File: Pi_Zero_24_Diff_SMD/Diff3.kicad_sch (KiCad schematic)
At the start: 14 parts, among them J10 Diff Out, J9 Diff Out, U10 AM26C31, U9 AM26C31

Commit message: generated WIP PCB
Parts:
- C10, C11: footprint (none) -> Capacitor_SMD:C_0603_1608Metric_Pad1.08x0.95mm_HandSolder
- J10, J9: footprint (none) -> Scotts:RJ45_Amphenol_54602-x08_Horizontal
- R22, R23, R24, R25, R26, R27, R28, R29: footprint (none) -> Resistor_SMD:R_0603_1608Metric_Pad0.98x0.95mm_HandSolder
- U10, U9: footprint (none) -> Package_SO:SOIC-16_3.9x9.9mm_P1.27mm
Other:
- title: Pi_Zero_24_Diff -> Pi Zero 24 Diff
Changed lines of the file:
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@@
   (paper "A4")
   (title_block
-    (title "Pi_Zero_24_Diff")
-    (date "2022-08-20")
+    (title "Pi Zero 24 Diff")
+    (date "2022-08-31")
     (rev "v1")
     (company "Scott Hanson")
@@
     (property "Reference" "J10" (id 0) (at 47.625 62.865 0))
     (property "Value" "Diff Out" (id 1) (at 48.895 64.77 0))
-    (property "Footprint" "" (id 2) (at 48.895 77.47 90)
+    (property "Footprint" "Scotts:RJ45_Amphenol_54602-x08_Horizontal" (id 2) (at 48.895 77.47 90)
       (effects (font (size 1.27 1.27)) hide)
     )
@@
     (property "Reference" "J9" (id 0) (at 49.7078 155.3718 0))
     (property "Value" "Diff Out" (id 1) (at 49.7078 153.0604 0))
-    (property "Footprint" "" (id 2) (at 48.26 139.065 90)
+    (property "Footprint" "Scotts:RJ45_Amphenol_54602-x08_Horizontal" (id 2) (at 48.26 139.065 90)
       (effects (font (size 1.27 1.27)) hide)
     )
@@
       (effects (font (size 1.27 1.27)) (justify left))
     )
-    (property "Footprint" "" (id 2) (at 60.96 106.172 90)
+    (property "Footprint" "Resistor_SMD:R_0603_1608Metric_Pad0.98x0.95mm_HandSolder" (id 2) (at 60.96 106.172 90)
       (effects (font (size 1.27 1.27)) hide)
     )
@@
       (effects (font (size 1.27 1.27)) (justify left))
     )
-    (property "Footprint" "" (id 2) (at 60.96 104.648 90)
+    (property "Footprint" "Resistor_SMD:R_0603_1608Metric_Pad0.98x0.95mm_HandSolder" (id 2) (at 60.96 104.648 90)
       (effects (font (size 1.27 1.27)) hide)
     )
@@
       (effects (font (size 1.27 1.27)) (justify left))
     )
-    (property "Footprint" "" (id 2) (at 60.96 121.793 90)
+    (property "Footprint" "Resistor_SMD:R_0603_1608Metric_Pad0.98x0.95mm_HandSolder" (id 2) (at 60.96 121.793 90)
       (effects (font (size 1.27 1.27)) hide)
     )
@@
       (effects (font (size 1.27 1.27)) (justify left))
     )
-    (property "Footprint" "" (id 2) (at 60.96 111.887 90)
+    (property "Footprint" "Resistor_SMD:R_0603_1608Metric_Pad0.98x0.95mm_HandSolder" (id 2) (at 60.96 111.887 90)
       (effects (font (size 1.27 1.27)) hide)
     )
@@
     (property "Reference" "U9" (id 0) (at 107.315 106.68 0))
     (property "Value" "AM26C31" (id 1) (at 107.315 108.9914 0))
-    (property "Footprint" "" (id 2) (at 112.395 147.955 0)
+    (property "Footprint" "Package_SO:SOIC-16_3.9x9.9mm_P1.27mm" (id 2) (at 112.395 147.955 0)
       (effects (font (size 1.27 1.27)) (justify left) hide)
     )
@@
       (effects (font (size 1.27 1.27)) (justify left))
     )
-    (property "Footprint" "" (id 2) (at 125.4252 114.935 0)
+    (property "Footprint" "Capacitor_SMD:C_0603_1608Metric_Pad1.08x0.95mm_HandSolder" (id 2) (at 125.4252 114.935 0)
       (effects (font (size 1.27 1.27)) hide)
     )
@@
       (effects (font (size 1.27 1.27)) (justify left))
     )
-    (property "Footprint" "" (id 2) (at 64.77 60.833 90)
+    (property "Footprint" "Resistor_SMD:R_0603_1608Metric_Pad0.98x0.95mm_HandSolder" (id 2) (at 64.77 60.833 90)
       (effects (font (size 1.27 1.27)) hide)
     )
@@
       (effects (font (size 1.27 1.27)) (justify left))
     )
-    (property "Footprint" "" (id 2) (at 129.2352 54.61 0)
+    (property "Footprint" "Capacitor_SMD:C_0603_1608Metric_Pad1.08x0.95mm_HandSolder" (id 2) (at 129.2352 54.61 0)
       (effects (font (size 1.27 1.27)) hide)
     )
@@
     (property "Reference" "U10" (id 0) (at 110.49 45.72 0))
     (property "Value" "AM26C31" (id 1) (at 110.49 48.0314 0))
-    (property "Footprint" "" (id 2) (at 115.57 86.995 0)
+    (property "Footprint" "Package_SO:SOIC-16_3.9x9.9mm_P1.27mm" (id 2) (at 115.57 86.995 0)
       (effects (font (size 1.27 1.27)) (justify left) hide)
     )
@@
       (effects (font (size 1.27 1.27)) (justify left))
     )
-    (property "Footprint" "" (id 2) (at 64.77 45.212 90)
+    (property "Footprint" "Resistor_SMD:R_0603_1608Metric_Pad0.98x0.95mm_HandSolder" (id 2) (at 64.77 45.212 90)
       (effects (font (size 1.27 1.27)) hide)
     )
@@
       (effects (font (size 1.27 1.27)) (justify left))
     )
-    (property "Footprint" "" (id 2) (at 64.77 43.688 90)
+    (property "Footprint" "Resistor_SMD:R_0603_1608Metric_Pad0.98x0.95mm_HandSolder" (id 2) (at 64.77 43.688 90)
       (effects (font (size 1.27 1.27)) hide)
     )
@@
       (effects (font (size 1.27 1.27)) (justify left))
     )
-    (property "Footprint" "" (id 2) (at 64.135 50.927 90)
-      (effects (font (size 1.27 1.27)) hide)
-    )
+    (property "Footprint" "Resistor_SMD:R_0603_1608Metric_Pad0.98x0.95mm_HandSolder" (id 2) (at 64.135 50.927 90)
+      (effects (font (size 1.27 1.27)) hide)
+    )

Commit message: working on routing
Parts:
- J7: renamed from J9; value Diff Out -> Diff Out 5
- J8: renamed from J10; value Diff Out -> Diff Out 6
- renumbered C10 to C8, C11 to C9, U9 to U7, U10 to U8
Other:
- moved on the sheet: C8, C9, J7, J8, R22, R23, R24, R25, R26, R27, R28, R29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

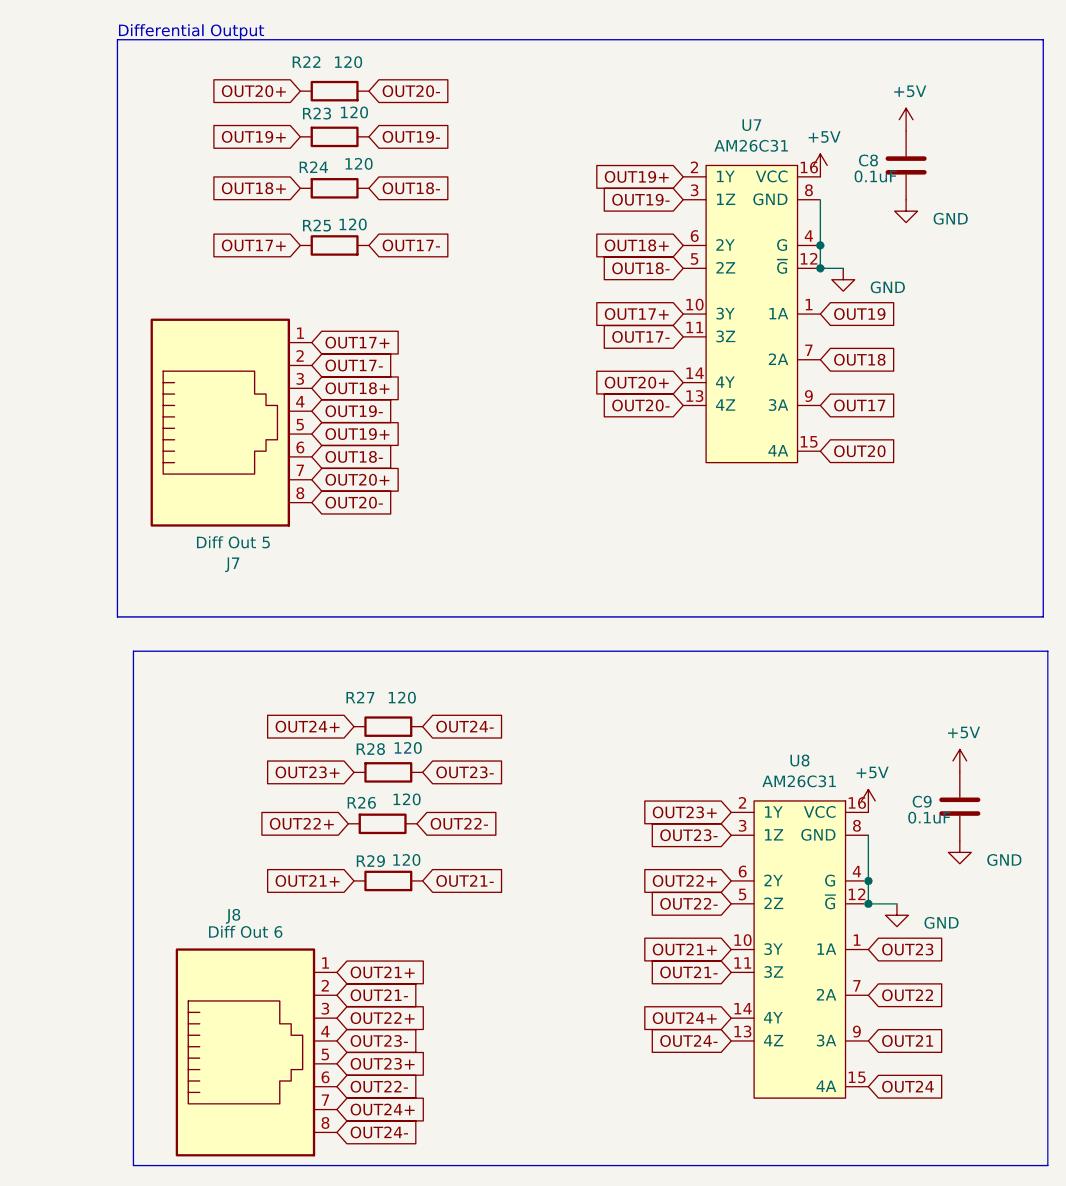
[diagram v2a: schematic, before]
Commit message: added PI Zero Diff
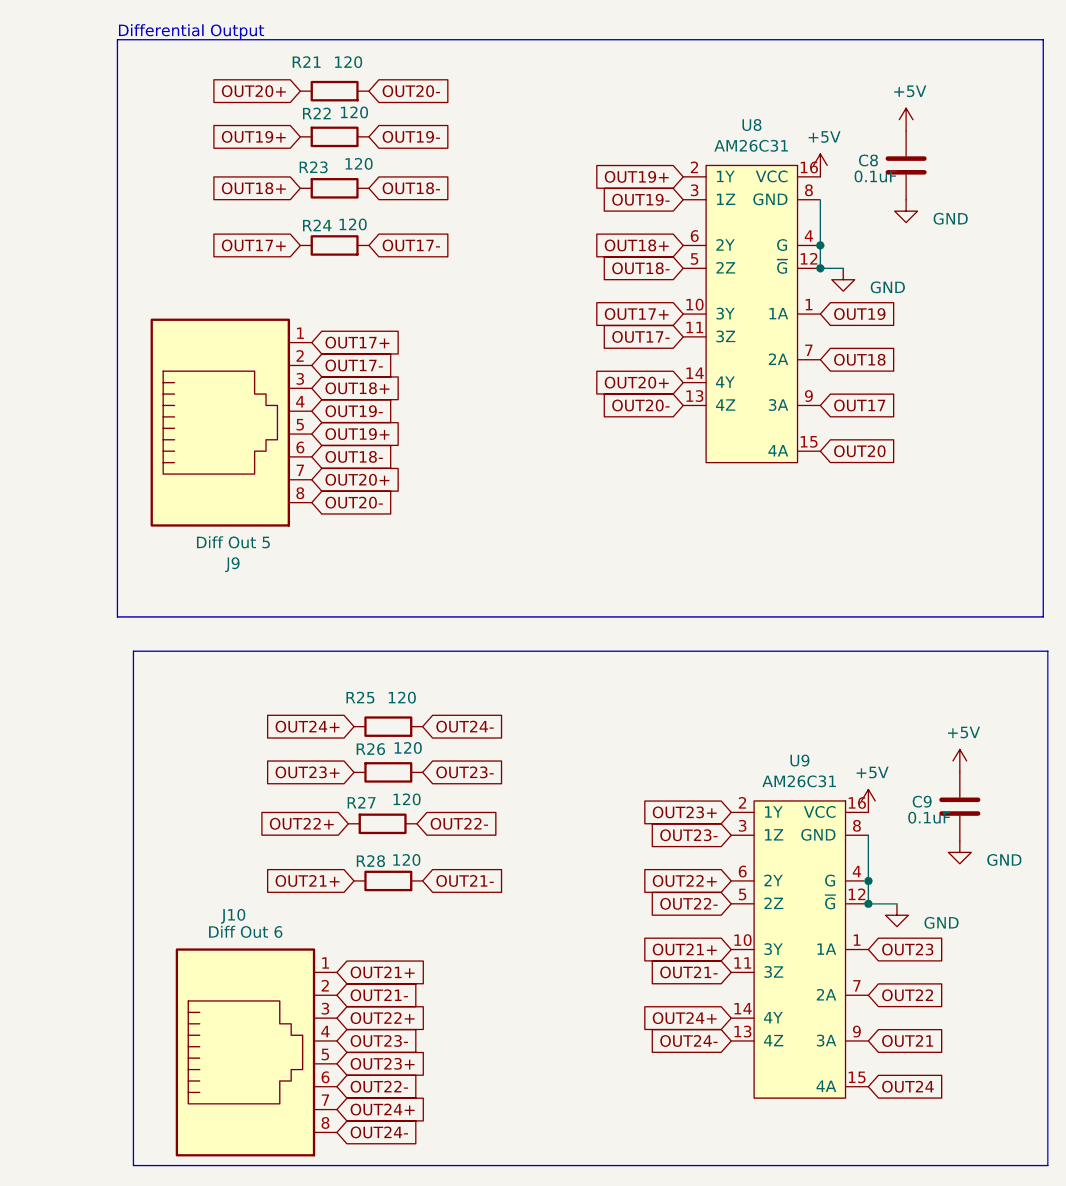
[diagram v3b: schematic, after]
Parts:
- J10: renamed from J8; LCSC C2938579 -> C86492
- J9: renamed from J7; LCSC C2938579 -> C86492
- renumbered R22 to R21, R23 to R22, R24 to R23, R25 to R24, R27 to R25, R28 to R26, R26 to R27, R29 to R28, U7 to U8, U8 to U9
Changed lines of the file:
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@@
   (symbol (lib_id "Connector:RJ45") (at 61.722 147.193 0) (mirror x) (unit 1)
     (in_bom yes) (on_board yes)
-    (property "Reference" "J8" (id 0) (at 60.452 133.223 0))
+    (property "Reference" "J10" (id 0) (at 60.452 133.223 0))
     (property "Value" "Diff Out 6" (id 1) (at 61.722 135.128 0))
     (property "Footprint" "Scotts:RJ45_Amphenol_54602-x08_Horizontal" (id 2) (at 61.722 147.828 90)
@@
       (effects (font (size 1.27 1.27)) hide)
     )
-    (property "LCSC" "C2938579" (id 6) (at 60.452 133.223 0)
+    (property "LCSC" "C86492" (id 6) (at 60.452 133.223 0)
       (effects (font (size 1.27 1.27)) hide)
     )
@@
   (symbol (lib_id "Connector:RJ45") (at 58.928 77.216 0) (mirror x) (unit 1)
     (in_bom yes) (on_board yes)
-    (property "Reference" "J7" (id 0) (at 60.3758 94.1578 0))
+    (property "Reference" "J9" (id 0) (at 60.3758 94.1578 0))
     (property "Value" "Diff Out 5" (id 1) (at 60.3758 91.8464 0))
     (property "Footprint" "Scotts:RJ45_Amphenol_54602-x08_Horizontal" (id 2) (at 58.928 77.851 90)
@@
       (effects (font (size 1.27 1.27)) hide)
     )
-    (property "LCSC" "C2938579" (id 6) (at 60.3758 94.1578 0)
+    (property "LCSC" "C86492" (id 6) (at 60.3758 94.1578 0)
       (effects (font (size 1.27 1.27)) hide)
     )
@@
   (symbol (lib_id "Device:R") (at 71.628 46.736 270) (unit 1)
     (in_bom yes) (on_board yes)
-    (property "Reference" "R23" (id 0) (at 67.945 44.196 90)
+    (property "Reference" "R22" (id 0) (at 67.945 44.196 90)
       (effects (font (size 1.27 1.27)) (justify left))
     )
@@
   (symbol (lib_id "Device:R") (at 71.628 41.656 90) (unit 1)
     (in_bom yes) (on_board yes)
-    (property "Reference" "R22" (id 0) (at 70.231 38.481 90)
+    (property "Reference" "R21" (id 0) (at 70.231 38.481 90)
       (effects (font (size 1.27 1.27)) (justify left))
     )
@@
   (symbol (lib_id "Device:R") (at 71.628 58.801 90) (unit 1)
     (in_bom yes) (on_board yes)
-    (property "Reference" "R25" (id 0) (at 71.374 56.642 90)
+    (property "Reference" "R24" (id 0) (at 71.374 56.642 90)
       (effects (font (size 1.27 1.27)) (justify left))
     )
@@
   (symbol (lib_id "Device:R") (at 71.628 52.451 270) (unit 1)
     (in_bom yes) (on_board yes)
-    (property "Reference" "R24" (id 0) (at 67.564 50.165 90)
+    (property "Reference" "R23" (id 0) (at 67.564 50.165 90)
       (effects (font (size 1.27 1.27)) (justify left))
     )
@@
   (symbol (lib_id "AM26C31:AM26C31") (at 117.983 66.421 0) (mirror y) (unit 1)
     (in_bom yes) (on_board yes)
-    (property "Reference" "U7" (id 0) (at 117.983 45.466 0))
+    (property "Reference" "U8" (id 0) (at 117.983 45.466 0))
     (property "Value" "AM26C31" (id 1) (at 117.983 47.7774 0))
     (property "Footprint" "Package_SO:SOIC-16_3.9x9.9mm_P1.27mm" (id 2) (at 123.063 86.741 0)
@@
   (symbol (lib_id "power:+5V") (at 125.603 51.181 0) (unit 1)
     (in_bom yes) (on_board yes)
-    (property "Reference" "#PWR048" (id 0) (at 125.603 54.991 0)
+    (property "Reference" "#PWR042" (id 0) (at 125.603 54.991 0)
       (effects (font (size 1.27 1.27)) hide)
     )
@@
   (symbol (lib_id "power:GND") (at 128.143 61.341 0) (unit 1)
     (in_bom yes) (on_board yes)
-    (property "Reference" "#PWR049" (id 0) (at 128.143 67.691 0)
+    (property "Reference" "#PWR044" (id 0) (at 128.143 67.691 0)
       (effects (font (size 1.27 1.27)) hide)
     )
@@
   (symbol (lib_id "power:+5V") (at 135.128 46.101 0) (unit 1)
     (in_bom yes) (on_board yes)
-    (property "Reference" "#PWR052" (id 0) (at 135.128 49.911 0)
+    (property "Reference" "#PWR041" (id 0) (at 135.128 49.911 0)
       (effects (font (size 1.27 1.27)) hide)
     )
@@
   (symbol (lib_id "power:GND") (at 135.128 53.721 0) (unit 1)
     (in_bom yes) (on_board yes)
-    (property "Reference" "#PWR053" (id 0) (at 135.128 60.071 0)
+    (property "Reference" "#PWR043" (id 0) (at 135.128 60.071 0)
       (effects (font (size 1.27 1.27)) hide)
     )
@@
   (symbol (lib_id "Device:R") (at 77.597 129.413 90) (unit 1)
     (in_bom yes) (on_board yes)
-    (property "Reference" "R29" (id 0) (at 77.343 127.254 90)
+    (property "Reference" "R28" (id 0) (at 77.343 127.254 90)
       (effects (font (size 1.27 1.27)) (justify left))
     )
@@
   (symbol (lib_id "power:+5V") (at 130.937 121.793 0) (unit 1)
     (in_bom yes) (on_board yes)
-    (property "Reference" "#PWR050" (id 0) (at 130.937 125.603 0)
+    (property "Reference" "#PWR046" (id 0) (at 130.937 125.603 0)
       (effects (font (size 1.27 1.27)) hide)
     )
@@
   (symbol (lib_id "power:+5V") (at 141.097 117.348 0) (unit 1)
     (in_bom yes) (on_board yes)
-    (property "Reference" "#PWR054" (id 0) (at 141.097 121.158 0)
+    (property "Reference" "#PWR045" (id 0) (at 141.097 121.158 0)
       (effects (font (size 1.27 1.27)) hide)
     )
@@
   (symbol (lib_id "AM26C31:AM26C31") (at 123.317 137.033 0) (mirror y) (unit 1)
     (in_bom yes) (on_board yes)
-    (property "Reference" "U8" (id 0) (at 123.317 116.078 0))
+    (property "Reference" "U9" (id 0) (at 123.317 116.078 0))
     (property "Value" "AM26C31" (id 1) (at 123.317 118.3894 0))
     (property "Footprint" "Package_SO:SOIC-16_3.9x9.9mm_P1.27mm" (id 2) (at 128.397 157.353 0)
@@
   (symbol (lib_id "Device:R") (at 77.597 117.348 270) (unit 1)
     (in_bom yes) (on_board yes)
-    (property "Reference" "R28" (id 0) (at 73.914 114.808 90)
+    (property "Reference" "R26" (id 0) (at 73.914 114.808 90)
       (effects (font (size 1.27 1.27)) (justify left))
     )
@@
   (symbol (lib_id "Device:R") (at 77.597 112.268 90) (unit 1)
     (in_bom yes) (on_board yes)
-    (property "Reference" "R27" (id 0) (at 76.2 109.093 90)
+    (property "Reference" "R25" (id 0) (at 76.2 109.093 90)
       (effects (font (size 1.27 1.27)) (justify left))
     )
@@
   (symbol (lib_id "power:GND") (at 141.097 124.968 0) (unit 1)
     (in_bom yes) (on_board yes)
-    (property "Reference" "#PWR055" (id 0) (at 141.097 131.318 0)
+    (property "Reference" "#PWR047" (id 0) (at 141.097 131.318 0)
       (effects (font (size 1.27 1.27)) hide)
     )
@@
   (symbol (lib_id "power:GND") (at 134.112 131.953 0) (unit 1)
     (in_bom yes) (on_board yes)
-    (property "Reference" "#PWR051" (id 0) (at 134.112 138.303 0)
+    (property "Reference" "#PWR048" (id 0) (at 134.112 138.303 0)
       (effects (font (size 1.27 1.27)) hide)
     )
@@
   (symbol (lib_id "Device:R") (at 76.962 123.063 270) (unit 1)
     (in_bom yes) (on_board yes)
-    (property "Reference" "R26" (id 0) (at 72.898 120.777 90)
-      (effects (font (size 1.27 1.27)) (justify left))
-    )
+    (property "Reference" "R27" (id 0) (at 72.898 120.777 90)
+      (effects (font (size 1.27 1.27)) (justify left))
+    )
